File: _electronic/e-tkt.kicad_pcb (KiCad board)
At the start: 4 copper layers, 99.6 x 76.2 mm, 109 parts, among them J1 Conn_01x03_Pin, J2 Conn_01x03_Pin, J3 Conn_01x03_Pin, J4 USB_C_Receptacle_PowerOnly_6P, U1 HUSB237-AA001-DN06R

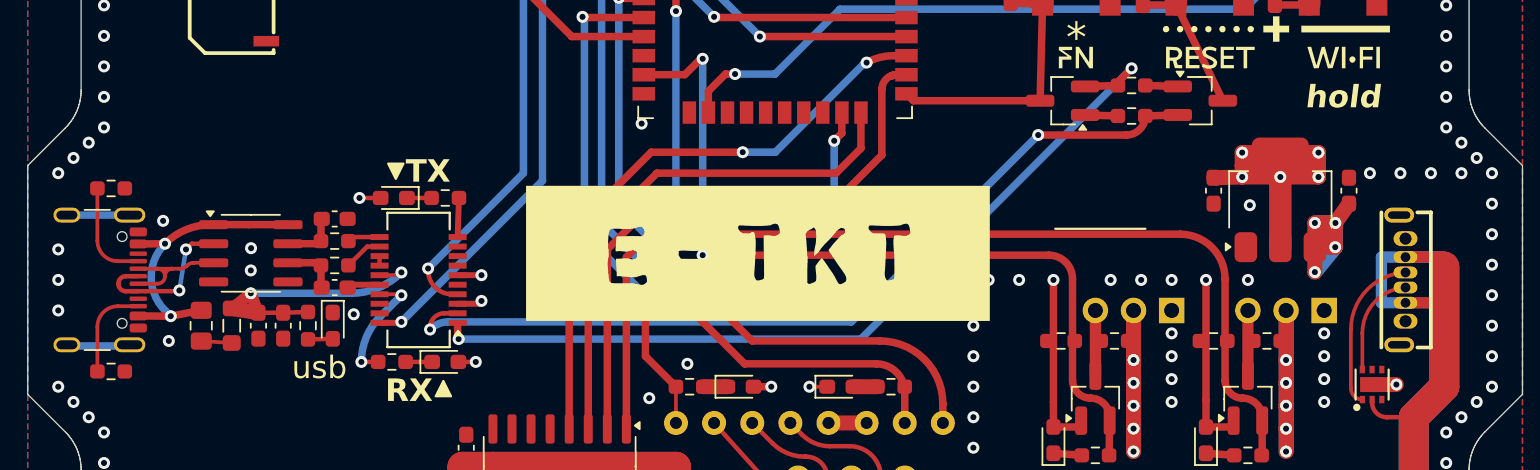
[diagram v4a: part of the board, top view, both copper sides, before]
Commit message: pillars F G optimized
for optional electronics cover and added M3 nut slots
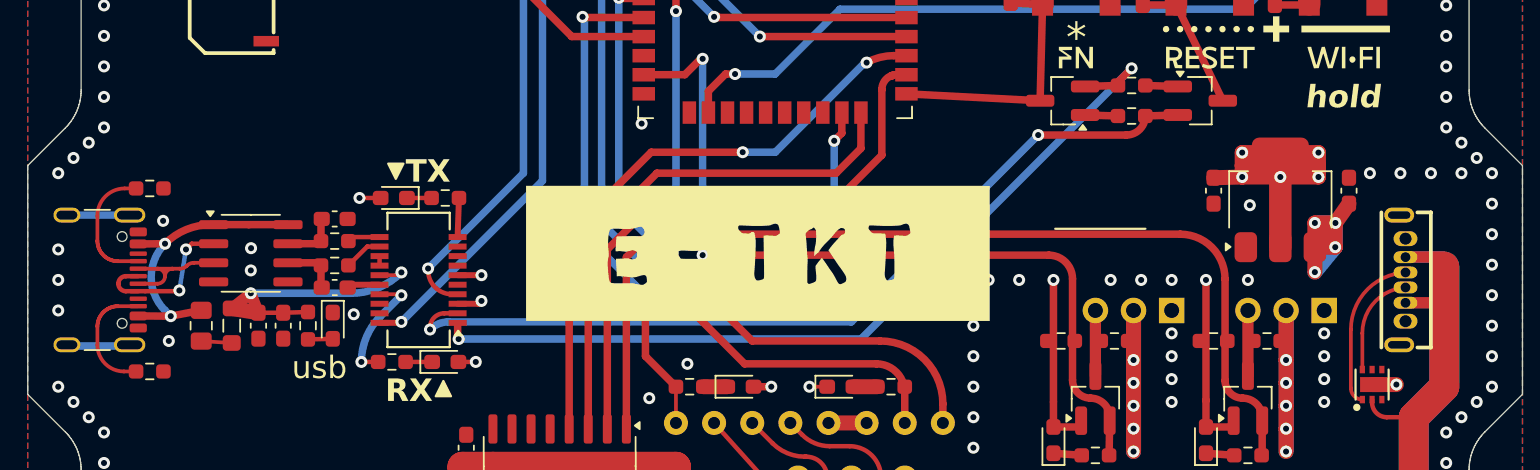
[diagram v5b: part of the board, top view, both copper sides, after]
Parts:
- moved R_USB1 2.58 mm to (136.7, -195.6)
- moved R_USB2 2.58 mm to (136.7, -183.4)
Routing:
- net +12V: track 314.8 -> 308.5 mm
- net Net-(J_USB1-CC2): track 6.43 -> 8.23 mm
- net Net-(J_USB1-CC1): track 6.93 -> 8.71 mm
